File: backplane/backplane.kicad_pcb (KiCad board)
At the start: 4 copper layers, 90 x 100 mm, 30 parts, among them J6 USB-C, U2 AP2112K-3.3

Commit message: RAM board attempt 2
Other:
- board text added: "RV2048 Backplane v0.1 © Michael Bell 2026 JLCJLCJLCJLC"

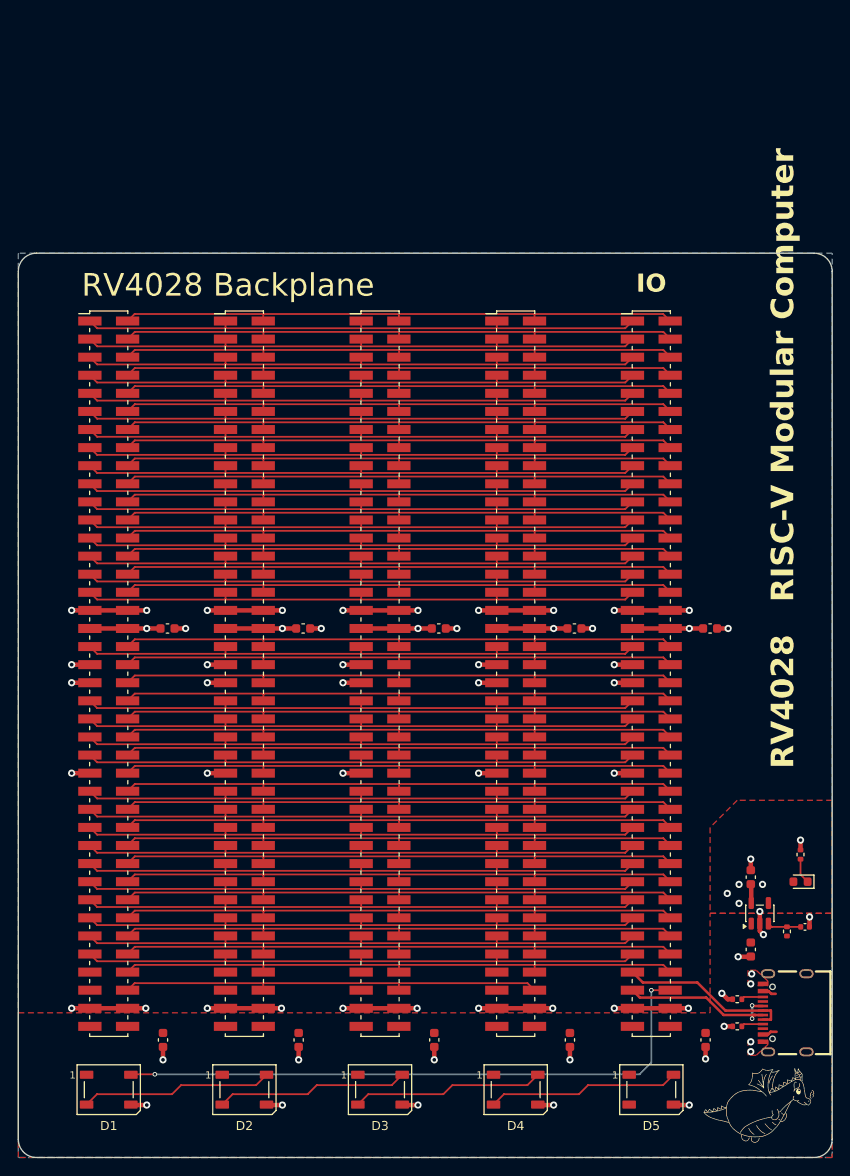
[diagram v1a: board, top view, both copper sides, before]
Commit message: Backplane reset and fixes
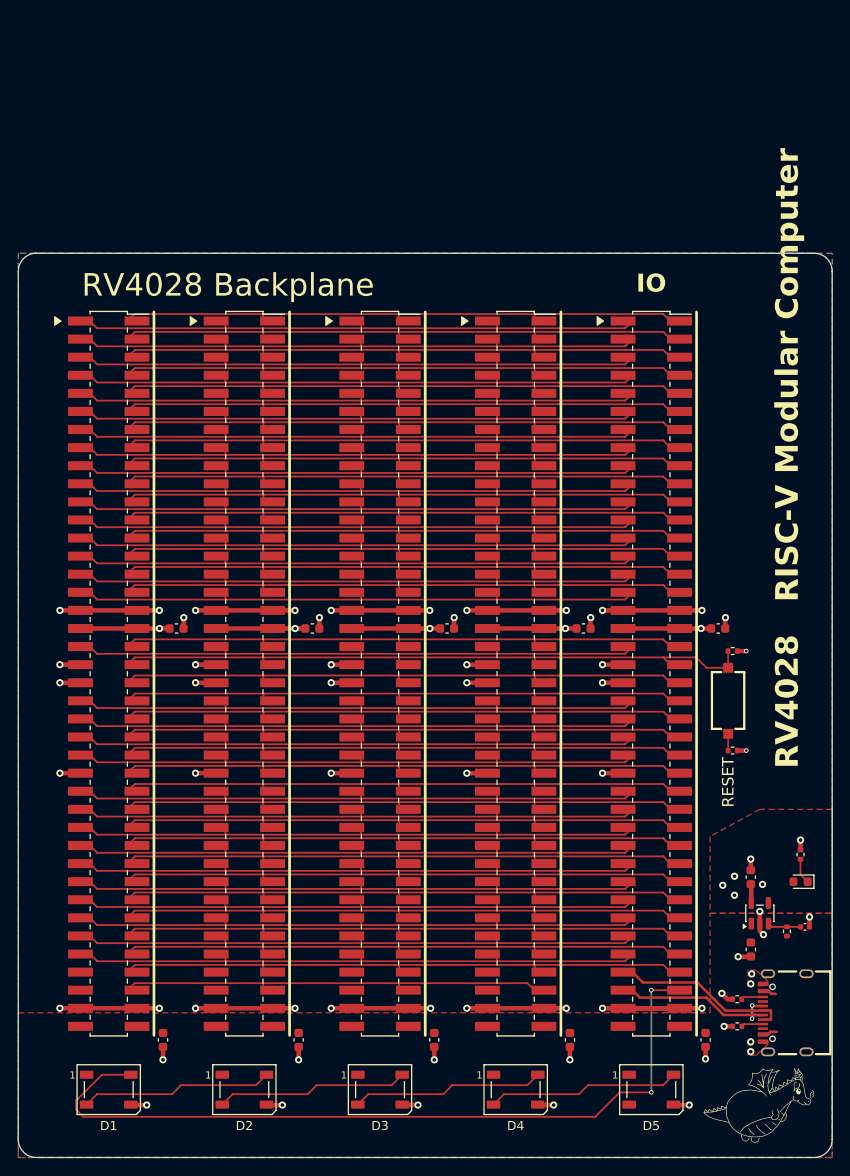
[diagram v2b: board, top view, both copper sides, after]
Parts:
- added R5: 47k, Resistor_SMD:R_0402_1005Metric, F.Cu at (119.0, 84.0)
- added R6: 1k, Resistor_SMD:R_0402_1005Metric, F.Cu at (119.0, 95.0)
- added SW1: RESET, RV4028:SW-SMD_HX-TS-1101-C-W, F.Cu at (118.5, 89.5)
- moved C4 1.01 mm to (72.5, 81.5)
- moved C3 1.00 mm to (57.5, 81.5)
- moved C6 1.00 mm to (102.5, 81.5)
- moved C5 0.91 mm to (87.4, 81.5)
- moved C7 0.90 mm to (117.4, 81.5)
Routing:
- net GND: track 144.8 -> 197.7 mm, vias 62 -> 63
- net Net-(D1-DIN): track 68.2 -> 86.7 mm
- net +3V3: track 41.2 -> 52.3 mm, vias 9 -> 10
- net ~{RST}: track 63.0 -> 72.0 mm
- net Net-(R6-Pad2): track 0.00 -> 1.85 mm

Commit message: Mounting holes
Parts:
- added H1: Hole, MountingHole:MountingHole_2.7mm_M2.5_DIN965_Pad, F.Cu at (43.0, 43.0)
- added H2: Hole, MountingHole:MountingHole_2.7mm_M2.5_DIN965_Pad, F.Cu at (127.0, 43.0)
- added H3: Hole, MountingHole:MountingHole_2.7mm_M2.5_DIN965_Pad, F.Cu at (127.0, 137.0)
- added H4: Hole, MountingHole:MountingHole_2.7mm_M2.5_DIN965_Pad, F.Cu at (43.0, 137.0)
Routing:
- net GND: track 197.7 -> 188.3 mm

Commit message: Review before first PCB order
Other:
- board text added: "RV4028 RISC-V Hackable Computer"
- board text removed: "RV4028 RISC-V Modular Computer"
